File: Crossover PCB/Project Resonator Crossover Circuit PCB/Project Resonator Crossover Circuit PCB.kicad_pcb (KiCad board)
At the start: 2 copper layers, 10 x 12.4 mm, 24 parts

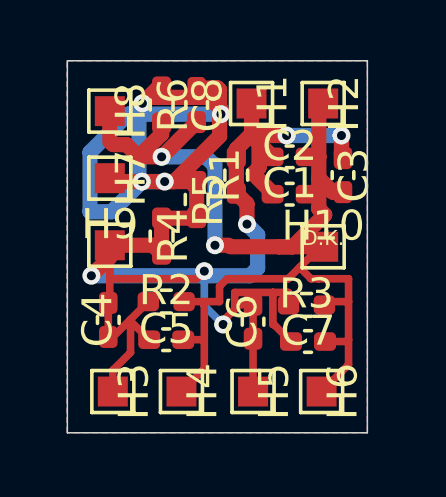
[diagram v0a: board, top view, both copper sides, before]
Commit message: MAJOR UPDATE: Improved Crossover to reduce redudent componets from 15 -> 10, Improved subbass isolation, updated PCB to reflect changes, added v3 shell images to assets, uploaded new gerber and drill files
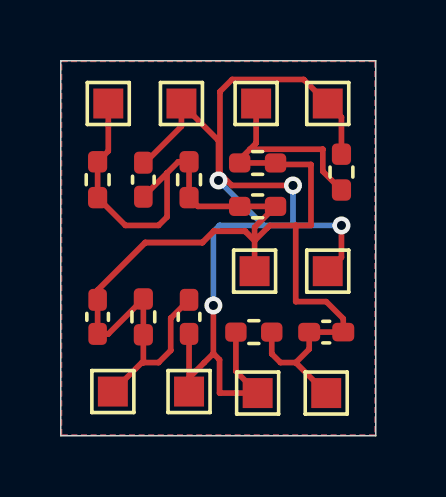
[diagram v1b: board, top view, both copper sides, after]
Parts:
- removed C2, C3: 100u, Capacitor_SMD:C_0402_1005Metric_Pad0.74x0.62mm_HandSolder
- removed C7: 2.2u, Capacitor_SMD:C_0402_1005Metric_Pad0.74x0.62mm_HandSolder
- removed C8: 10u, Capacitor_SMD:C_0402_1005Metric_Pad0.74x0.62mm_HandSolder
- added R7: 500R, Resistor_SMD:R_0402_1005Metric_Pad0.72x0.64mm_HandSolder, F.Cu at (165.1, 54.9)
- C1: value 100u -> 10u
- C4: value 0.027u -> 0.056u
- C6: value 0.008u -> 0.018u
- R1: value 5600R -> 800R
- R2: value 22R -> 56R
- R3: value 10000R -> 22R
- R4: value 6800R -> 800R
- R5: value 0.092R -> 800R
- R6: value 6.8R -> 0.22R
- moved R6 6.40 mm to (173.2, 54.6), turned to 90 degrees
- moved H9 4.90 mm to (170.3, 57.9)
- moved C1 4.90 mm to (166.6, 54.9), turned to 90 degrees
- moved R4 4.02 mm to (170.4, 54.3), turned to 0 degrees
- moved H7 2.49 mm to (165.5, 52.3)
- moved C6 2.46 mm to (172.7, 59.9), turned to 0 degrees
- moved H5 2.44 mm to (172.7, 62.0)
- moved H8 2.40 mm to (167.9, 52.3)
- moved H6 2.13 mm to (170.4, 62.0)
- moved R5 2.04 mm to (170.4, 55.8), turned to 0 degrees
- moved R3 1.98 mm to (170.3, 59.9), turned to 180 degrees
- moved R1 1.58 mm to (168.1, 54.9)
- moved C5 1.08 mm to (168.1, 59.4), turned to -90 degrees
- moved R2 0.92 mm to (166.6, 59.4), turned to 90 degrees
- moved H10 0.83 mm to (172.8, 57.9)
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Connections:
- R2 pad 2: GND -> +
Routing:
- net +: track 72.2 -> 55.3 mm, vias 10 -> 0
- net GND: track 39.4 -> 39.1 mm, vias 2 -> 4
- added copper zone on B.Cu, net Net-(C1-Pad2)
- added copper zone on F.Cu, net Net-(C1-Pad2)
- removed copper zone on B.Cu, net GND
- removed copper zone on F.Cu, net GND
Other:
- board size 10 x 12.4 mm -> 10.5 x 12.5 mm
- board text removed: "D.K."

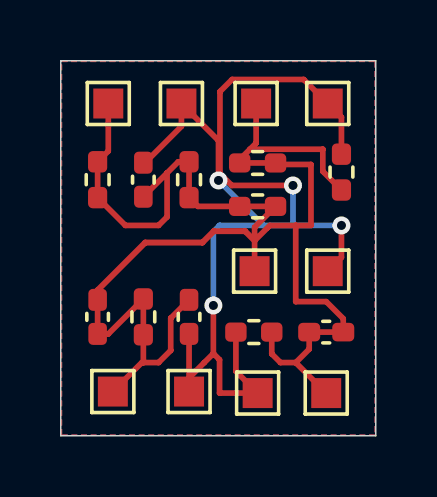
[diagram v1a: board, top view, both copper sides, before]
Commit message: updated PCB to connect ground pour to GND and make track size to 8mils and fixed clearence issues
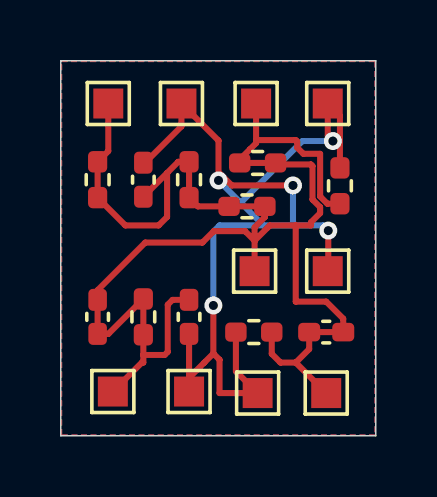
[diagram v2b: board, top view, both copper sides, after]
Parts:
- moved R6 0.46 mm to (173.2, 55.1)
- moved R5 0.36 mm to (170.1, 55.8)
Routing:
- net GND: track 39.1 -> 37.2 mm, vias 4 -> 5
- net +: track 55.3 -> 55.9 mm
- added copper zone on B.Cu, net GND
- added copper zone on F.Cu, net GND
- removed copper zone on B.Cu, net Net-(C1-Pad2)
- removed copper zone on F.Cu, net Net-(C1-Pad2)

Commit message: updated 800ohm to 750ohm for product resistor in use from JLCPCB, updated ground and added 1 more resistor for CI driver, updated gerber and drill files and updated crossover ciruit to match changes
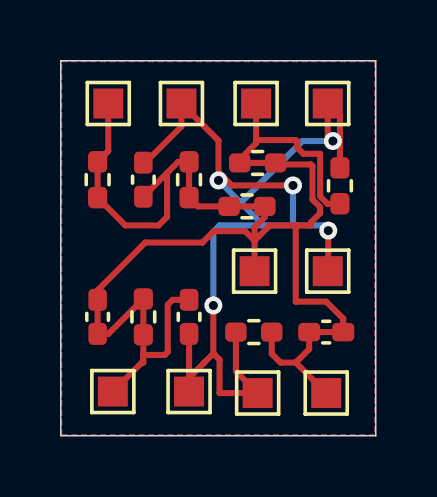
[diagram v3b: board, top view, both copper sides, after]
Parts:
- C1: value 10u -> 10uF
- C4: value 0.056u -> 0.039uF
- C5: value 4.7u -> 4.7uF
- C6: value 0.018u -> 0.012uF
- R2: value 56R -> 300R
- R7: value 500R -> 800R
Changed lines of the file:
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@@
 			)
 		)
-		(property "Value" "0.056u"
+		(property "Value" "0.039uF"
 			(at 0 1.16 90)
 			(layer "F.Fab")
@@
 			)
 		)
-		(property "Value" "500R"
+		(property "Value" "800R"
 			(at 0 1.17 90)
 			(layer "F.Fab")
@@
 			)
 		)
-		(property "Value" "56R"
+		(property "Value" "300R"
 			(at 0 1.17 90)
 			(layer "F.Fab")
@@
 			)
 		)
-		(property "Value" "0.018u"
+		(property "Value" "0.012uF"
 			(at 0 1.16 0)
 			(layer "F.Fab")
@@
 			)
 		)
-		(property "Value" "4.7u"
+		(property "Value" "4.7uF"
 			(at 0 1.16 90)
 			(layer "F.Fab")
@@
 			)
 		)
+		(property "LCSC" ""
+			(at 0 0 0)
+			(layer "F.SilkS")
+			(hide yes)
+			(effects
+				(font
+					(size 1.27 1.27)
+					(thickness 0.15)
+				)
+			)
+		)
 		(property ki_fp_filters "C_*")
 		(sheetname "/")
@@
 			)
 		)
-		(property "Value" "10u"
+		(property "Value" "10uF"
 			(at 0 1.16 90)
 			(layer "F.Fab")
@@
 			)
 		)
+		(property "LCSC" ""
+			(at 0 0 0)
+			(layer "F.SilkS")
+			(hide yes)
+			(effects
+				(font
+					(size 1.27 1.27)
+					(thickness 0.15)
+				)
+			)
+		)
 		(property ki_fp_filters "C_*")
 		(sheetname "/")
@@
 		(start 173.1772 54.4697)
 		(end 173.1772 52.7304)
-		(width 0.2)
+		(width 0.2032)
 		(layer "F.Cu")
 		(net 1)
@@
 		(start 173.1772 52.7304)
 		(end 172.7708 52.324)
-		(width 0.2)
+		(width 0.2032)
 		(layer "F.Cu")
 		(net 1)
@@
 		(start 172.7708 53.403608)
 		(end 172.942196 53.575004)
-		(width 0.2)
+		(width 0.2032)
 		(layer "F.Cu")
 		(net 1)
@@
 		(start 172.7708 52.324)
 		(end 172.7708 53.403608)
-		(width 0.2)
+		(width 0.2032)
 		(layer "F.Cu")
 		(net 1)
@@
 		(start 172.942196 53.575004)
 		(end 171.926196 53.575004)
-		(width 0.2)
+		(width 0.2032)
 		(layer "B.Cu")
 		(net 1)
@@
 		(start 171.926196 53.575004)
 		(end 169.871256 55.629944)
-		(width 0.2)
+		(width 0.2032)
 		(layer "B.Cu")
 		(net 1)
@@
 		(start 167.4368 60.6044)
 		(end 167.3352 60.706)
-		(width 0.2)
+		(width 0.2032)
 		(layer "F.Cu")
 		(net 2)
@@
 		(start 167.4368 59.0296)
 		(end 167.4368 60.6044)
-		(width 0.2)
+		(width 0.2032)
 		(layer "F.Cu")
 		(net 2)
@@
 		(start 167.3352 60.706)
 		(end 166.624 60.706)
-		(width 0.2)
+		(width 0.2032)
 		(layer "F.Cu")
 		(net 2)
@@
 		(start 168.148 58.8685)
 		(end 167.5979 58.8685)
-		(width 0.2)
+		(width 0.2032)
 		(layer "F.Cu")
 		(net 2)
@@
 		(start 167.5979 58.8685)
 		(end 167.4368 59.0296)
-		(width 0.2)
+		(width 0.2032)
 		(layer "F.Cu")
 		(net 2)

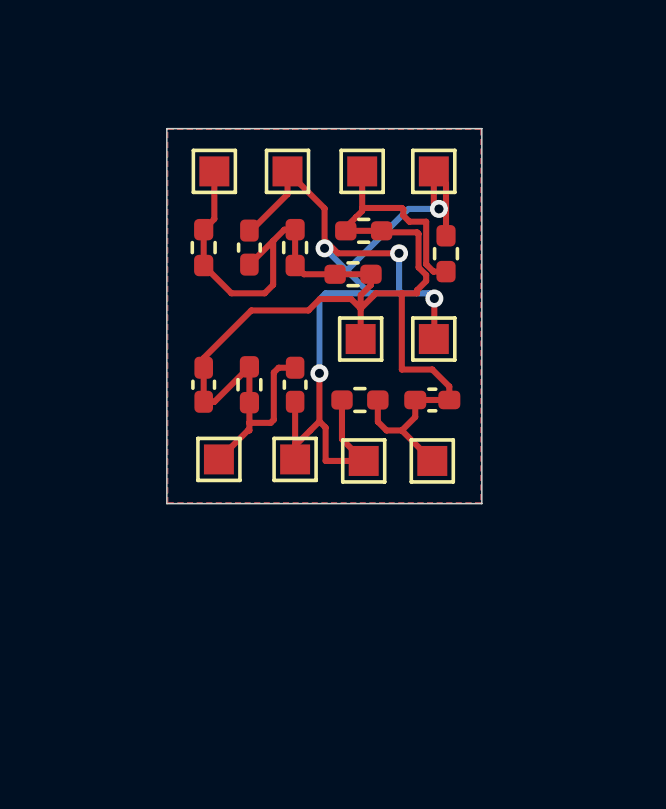
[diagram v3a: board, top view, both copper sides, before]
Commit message: Redesigned Layout of PCB to Wrap Shell, Updated Overall Shell Design, Removed Bluetooth Code experimental, Rendered New colorways mockups
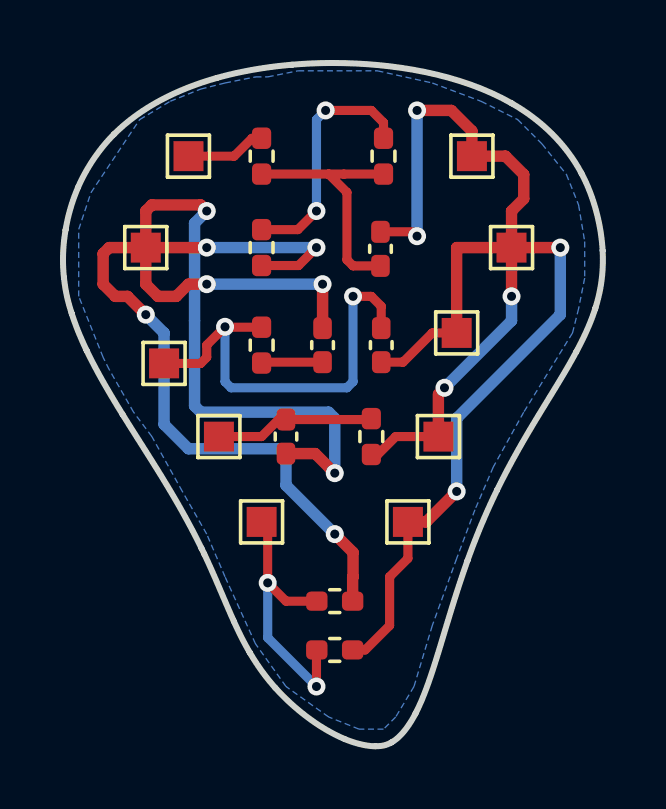
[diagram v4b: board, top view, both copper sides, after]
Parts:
- H9: value + MountingHole_Pad -> + CI MNT
- moved R6 13.7 mm to (169.5, 68.3), turned to 0 degrees
- moved R4 12.4 mm to (169.5, 66.6)
- moved H8 12.4 mm to (171.9, 64.0)
- moved H1 12.2 mm to (167.0, 64.0)
- moved H9 7.78 mm to (163.2, 54.9)
- moved H5 7.16 mm to (165.6, 61.2)
- moved H4 6.84 mm to (173.5, 57.7)
- moved C6 5.03 mm to (167.8, 61.2), turned to -90 degrees
- moved C1 4.37 mm to (171.0, 54.9)
- moved R1 4.24 mm to (171.1, 51.8), turned to 90 degrees
- moved C4 4.18 mm to (169.1, 58.1)
- moved H10 4.00 mm to (175.4, 54.9)
- moved H3 3.69 mm to (163.8, 58.7)
- moved R7 3.61 mm to (167.0, 51.8), turned to -90 degrees
- moved R5 3.18 mm to (167.0, 54.9), turned to -90 degrees
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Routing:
- net +: track 55.9 -> 105.2 mm, vias 0 -> 14
- net GND: track 37.2 -> 48.9 mm, vias 5 -> 6
- removed copper zone on F.Cu, net GND
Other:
- board size 10.5 x 12.5 mm -> 18 x 22.8 mm

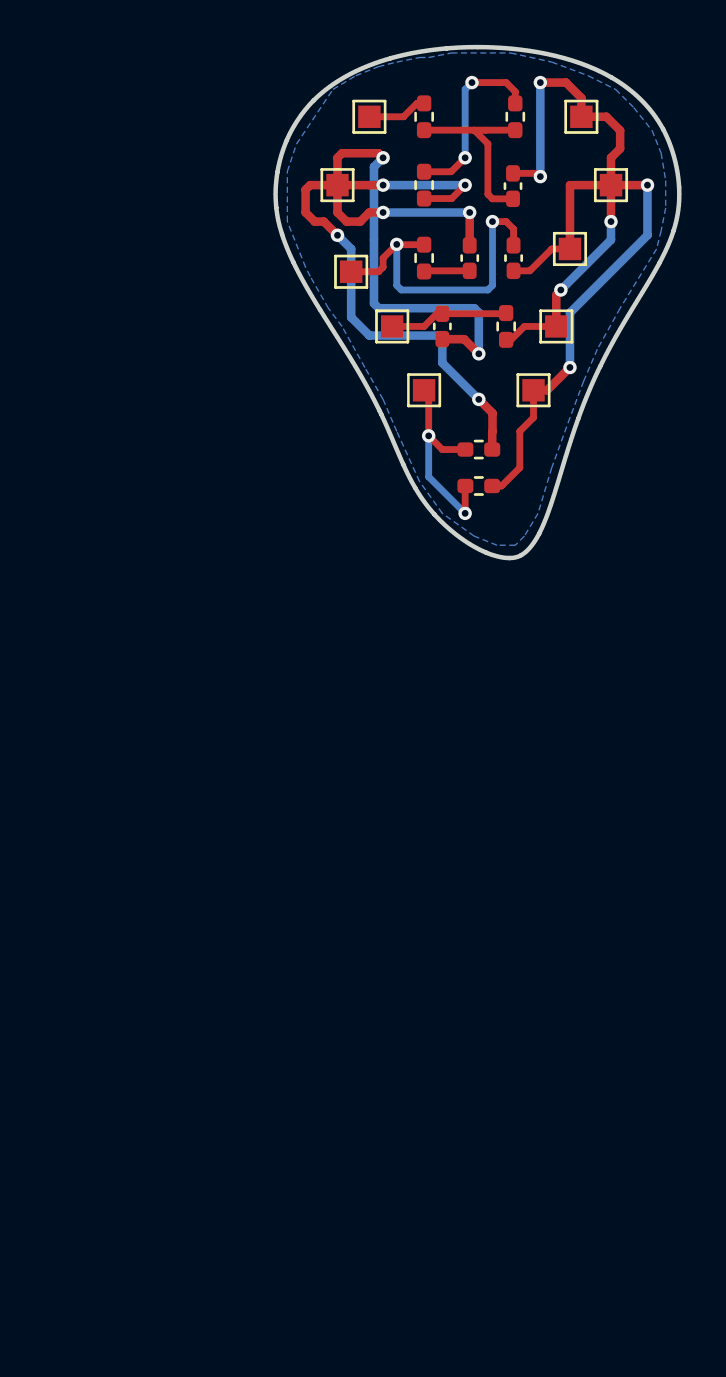
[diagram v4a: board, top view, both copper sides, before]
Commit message: updated PCB crossover to match the latest crossover diagram and fixed size to fit latest version of the shell
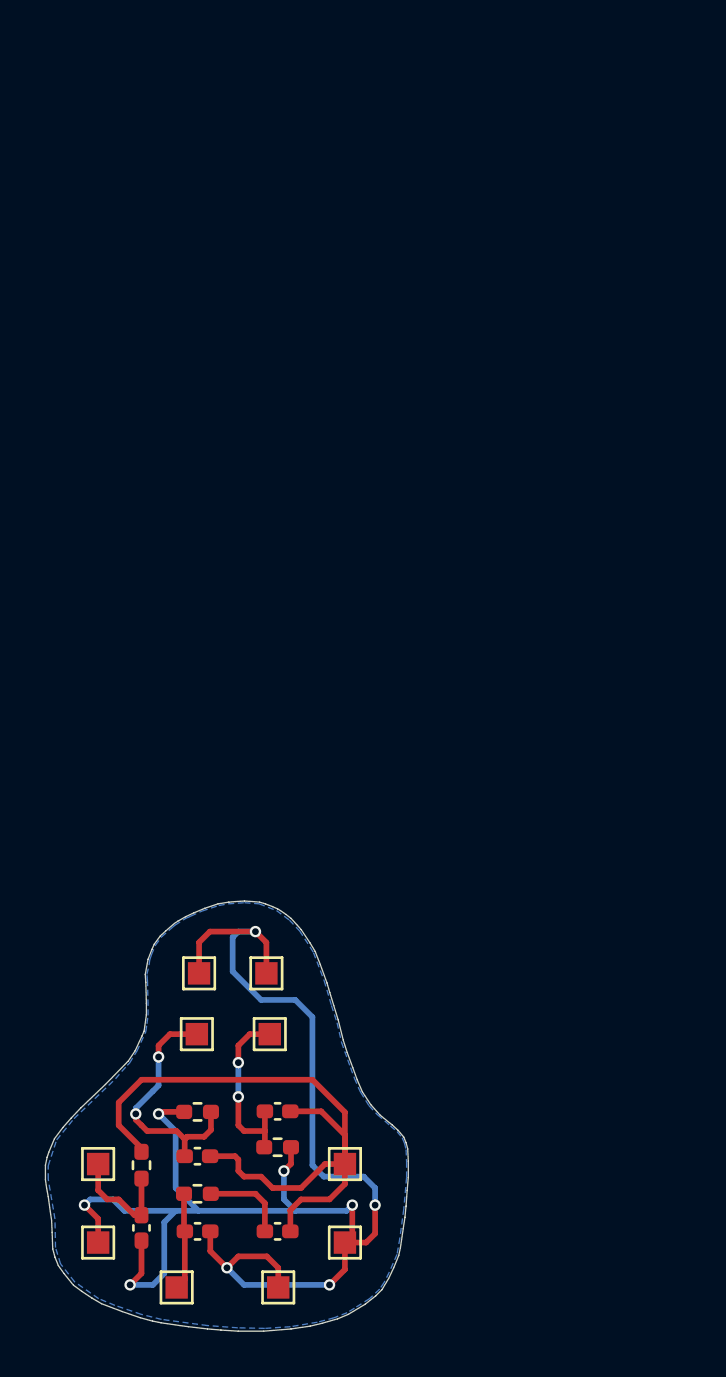
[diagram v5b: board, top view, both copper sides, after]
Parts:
- removed R1, R4, R7: 800R, Resistor_SMD:R_0402_1005Metric_Pad0.72x0.64mm_HandSolder
- added C2: 2.2uF, Capacitor_SMD:C_0402_1005Metric_Pad0.74x0.62mm_HandSolder, F.Cu at (156.9, 98.2)
- C4: value 0.039uF -> 0.10uF
- C6: value 0.012uF -> 2.2uF
- H1: value + MountingHole_Pad -> CI PAD (+)
- H10: value MountingHole_Pad -> SOURCE PAD (-)
- H2: value - MountingHole_Pad -> CI PAD (-)
- H3: value + MountingHole_Pad -> BK PAD (+)
- H4: value - MountingHole_Pad -> BK PAD (-)
- H5: value + MountingHole_Pad -> SWFK #1 PAD (+)
- H6: value - MountingHole_Pad -> SWFK #1 PAD (-)
- H7: value + MountingHole_Pad -> SWFK #2 PAD (+)
- H8: value - MountingHole_Pad -> SWFK #2 PAD (-)
- H9: value + CI MNT -> SOURCE PAD (+)
- R2: value 300R -> 22R
- R3: value 22R -> 6.8R
- R5: value 800R -> 22R
- R6: value 0.22R -> 22R
- moved H2 54.6 mm to (152.5, 102.0), turned to 0 degrees
- moved C1 49.3 mm to (154.4, 101.3), turned to -90 degrees
- moved H10 48.6 mm to (163.5, 102.0), turned to 90 degrees
- moved H4 48.1 mm to (160.5, 104.0), turned to 0 degrees
- moved H3 45.9 mm to (156.0, 104.0), turned to 0 degrees
- moved C5 45.6 mm to (156.9, 101.5), turned to 0 degrees
- moved R5 45.5 mm to (154.4, 98.6), turned to 90 degrees
- moved C4 44.2 mm to (160.5, 101.5), turned to 0 degrees
- moved H9 43.6 mm to (163.5, 98.5), turned to 90 degrees
- moved R2 42.9 mm to (156.9, 99.8), turned to 0 degrees
- moved H7 41.6 mm to (156.9, 92.7), turned to 90 degrees
- moved R3 38.0 mm to (160.5, 97.8), turned to 0 degrees
- moved H1 37.4 mm to (152.5, 98.5), turned to 0 degrees
- moved C6 35.7 mm to (160.5, 96.2), turned to 0 degrees
- moved H5 32.0 mm to (160.2, 92.7), turned to 0 degrees
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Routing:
- net +: track 105.2 -> 64.8 mm, vias 14 -> 4
- net GND: track 48.9 -> 71.7 mm, vias 6 -> 9
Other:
- board size 18 x 22.8 mm -> 16.2 x 19.2 mm
